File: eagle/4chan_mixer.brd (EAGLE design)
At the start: 100 x 80 mm, 29 parts, among them IC1 TL072P

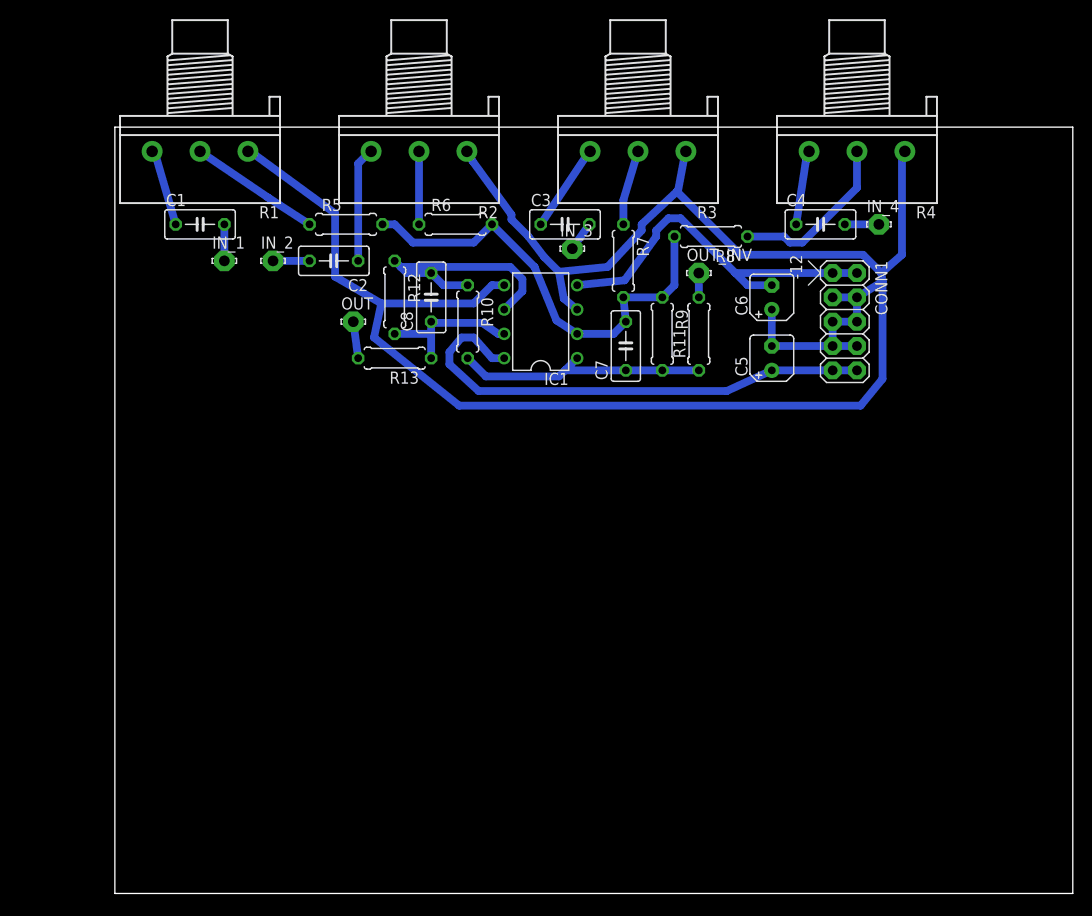
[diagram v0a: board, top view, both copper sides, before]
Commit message: grounds and cutout path for cnc
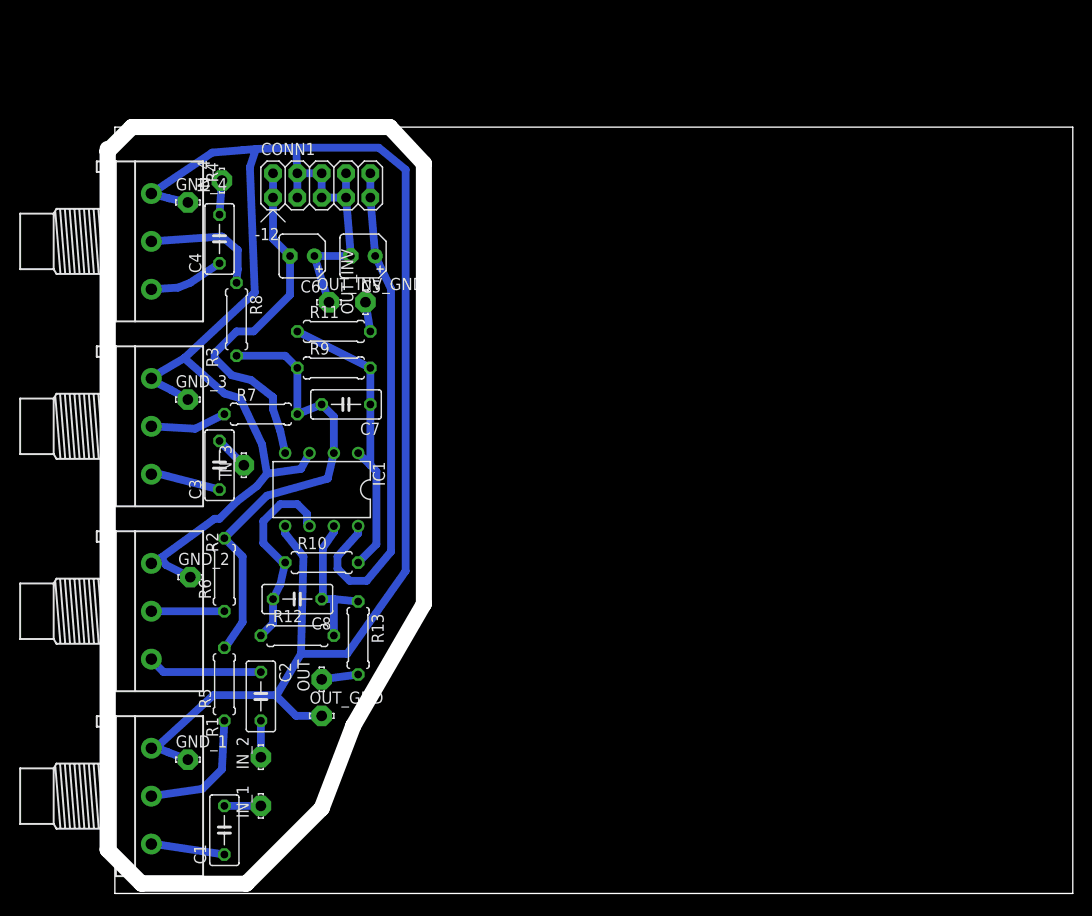
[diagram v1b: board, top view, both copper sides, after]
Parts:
- added GND_1, GND_2, GND_3, GND_4, OUT_GND, OUT_INV_GND: LSP11, solpad:LSP11
- moved R4 74.3 mm to (3.81, 68.1), turned to 270 degrees
- moved IN_4 68.7 mm to (11.2, 74.4), turned to 90 degrees
- moved R1 67.5 mm to (3.81, 10.2), turned to 270 degrees
- moved C1 63.3 mm to (11.4, 6.60), turned to 90 degrees
- moved C4 62.8 mm to (10.9, 68.3), turned to 90 degrees
- moved R3 58.3 mm to (3.81, 48.8), turned to 270 degrees
- moved IN_1 57.0 mm to (15.2, 9.14), turned to 90 degrees
- moved CONN1 56.4 mm to (21.6, 73.9), turned to 0 degrees
- moved R2 55.5 mm to (3.81, 29.5), turned to 270 degrees
- moved IN_2 51.8 mm to (15.2, 14.2), turned to 90 degrees
- moved R8 50.3 mm to (12.7, 59.9), turned to 270 degrees
- moved R5 49.7 mm to (11.4, 21.8), turned to 90 degrees
- moved C6 49.2 mm to (19.6, 66.5), turned to 180 degrees
- moved C2 46.1 mm to (15.2, 20.6), turned to 270 degrees
- moved C5 44.0 mm to (25.9, 66.5), turned to 180 degrees
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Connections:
- net GND: now also GND_1.MP, GND_2.MP, GND_3.MP, GND_4.MP, OUT_GND.MP, OUT_INV_GND.MP
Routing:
- net GND: track 214.5 -> 239.9 mm
- net N$4: track 25.9 -> 20.9 mm
- net N$12: track 17.9 -> 13.0 mm
- net N$17: track 27.0 -> 31.7 mm
- net N$8: track 9.24 -> 7.39 mm
- net -12V: track 39.4 -> 37.9 mm
- net N$16: track 47.0 -> 48.5 mm
- net N$18: track 2.54 -> 3.09 mm
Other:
- board size 100 x 80 mm -> 100.8 x 80 mm

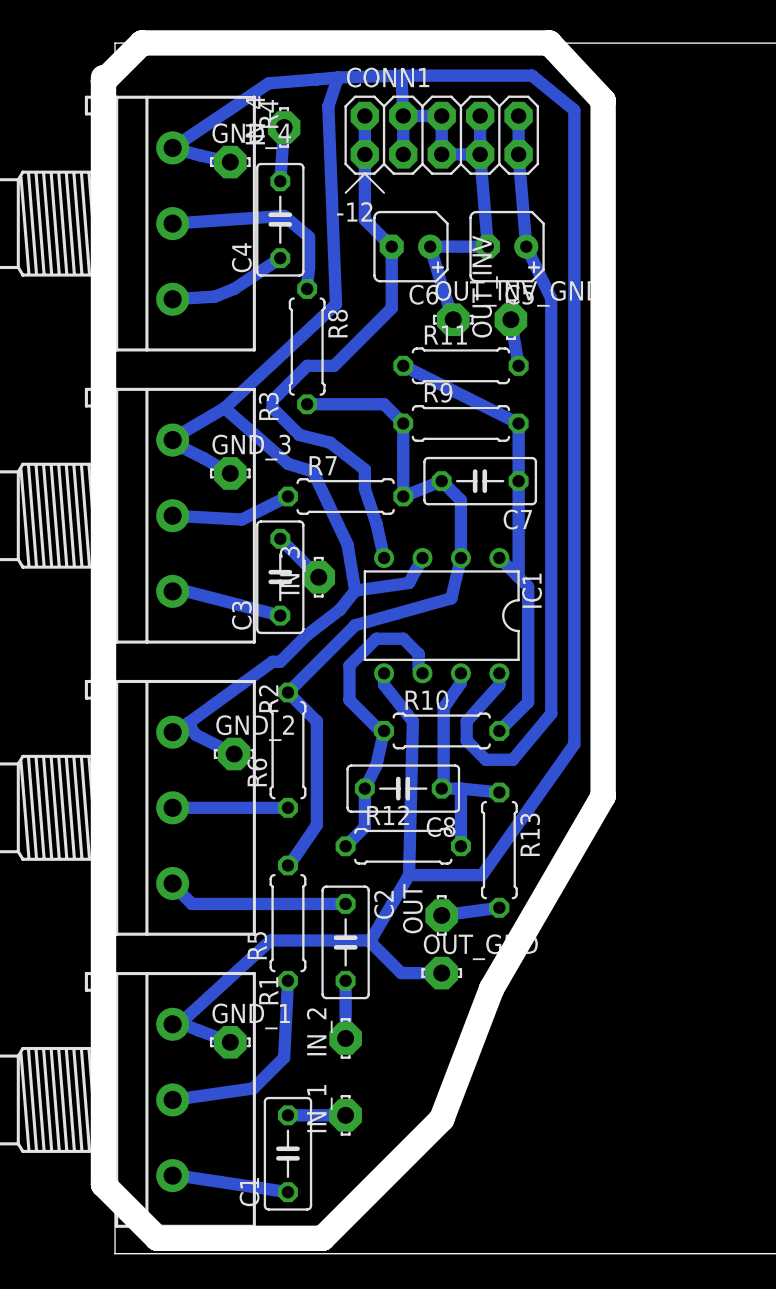
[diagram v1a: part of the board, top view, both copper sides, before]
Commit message: now with ferrite bead filters and decouple caps closer to opamp
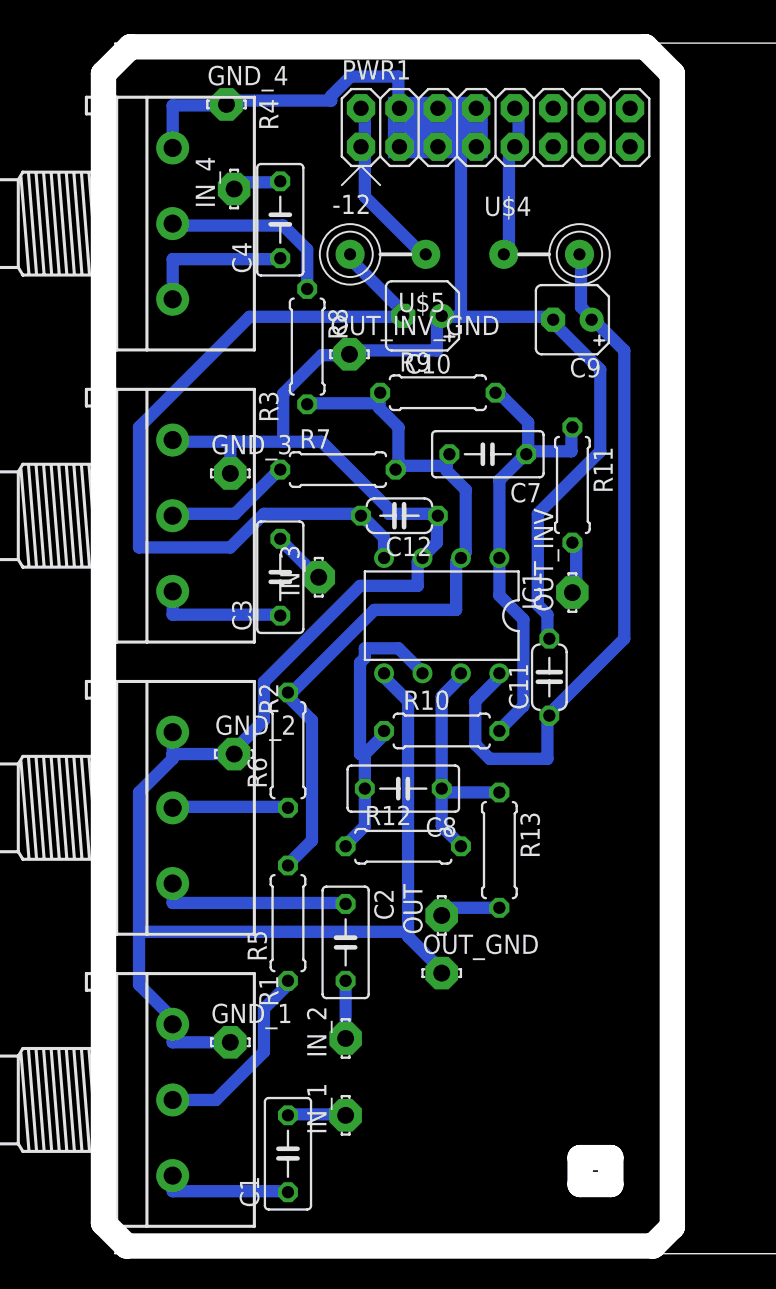
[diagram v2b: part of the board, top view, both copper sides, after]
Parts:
- removed C5, C6: 1uF, rcl:B45181A
- removed CONN1: POWER_SIMPLE10, eurorack:POWER_10
- added C10, C9: 10u, rcl:B45181A
- added C11, C12: 100n, rcl:C050-024X044
- added PWR1: POWER, eurorack:POWER_16
- added U$4, U$5: FB, adafruit:FB
- moved OUT_INV 18.5 mm to (30.2, 43.7)
- moved R11 10.8 mm to (30.2, 50.8), turned to 270 degrees
- moved OUT_INV_GND 7.23 mm to (15.5, 59.4)
- moved IN_4 5.24 mm to (7.87, 70.4)
- moved GND_4 3.82 mm to (7.37, 75.9)
- moved R9 2.54 mm to (21.3, 56.9)
- moved R7 1.85 mm to (14.7, 51.8)
- moved C7 1.85 mm to (24.6, 52.8)
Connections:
- new net N$20: PWR1.1, PWR1.2, U$5.P$1
- new net N$6: PWR1.10, PWR1.9, U$4.P$1
- net +12V: now also C11.1, C9.+, U$4.P$2; no longer C5.+, CONN1.10, CONN1.9
- net -12V: now also C10.-, C12.2, U$5.P$2; no longer C6.-, CONN1.1, CONN1.2
- net GND: now also C10.+, C11.2, C12.1, C9.-, PWR1.3, PWR1.4, PWR1.5, PWR1.6, PWR1.7, PWR1.8; no longer C5.-, C6.+, CONN1.3, CONN1.4, CONN1.5, CONN1.6, CONN1.7, CONN1.8
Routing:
- net GND: track 239.9 -> 209.3 mm
- net -12V: track 37.9 -> 53.0 mm
- net N$20: track 0.00 -> 11.9 mm
- net N$6: track 0.00 -> 10.4 mm
- net +12V: track 52.7 -> 47.3 mm
- net N$16: track 48.5 -> 51.3 mm
- net N$11: track 7.83 -> 9.78 mm
- net N$17: track 31.7 -> 30.2 mm
- net N$8: track 7.39 -> 8.67 mm
- net N$5: track 15.6 -> 16.4 mm
- net N$2: track 12.0 -> 12.8 mm
- net N$12: track 13.0 -> 12.3 mm
- net N$15: track 13.3 -> 12.7 mm
- net N$14: track 8.07 -> 8.72 mm
- net N$18: track 3.09 -> 3.71 mm
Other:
- outline, holes or cut-outs redrawn
